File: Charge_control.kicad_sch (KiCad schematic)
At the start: 6 parts, among them Q13 Q_NMOS_SDG, Q14 Q_NMOS_SDG, U3 BQ76200PW

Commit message: update
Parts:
- added C? (x2): 100n, Capacitor_SMD:C_0805_2012Metric, symbol Device:C
- added C?: 100n, symbol Device:C_Small
- added C?: 10n, Capacitor_SMD:C_0805_2012Metric, symbol Device:C
- added D?: D_Zener, symbol Device:D_Zener
- added J4: Conn_01x05, Connector_PinSocket_2.54mm:PinSocket_1x05_P2.54mm_Vertical, symbol Connector_Generic:Conn_01x05
- added Q?: BSS84, Package_TO_SOT_SMD:SOT-23, symbol Transistor_FET:BSS84
- added Q?: Q_NMOS_SDG, symbol Device:Q_NMOS_SDG
- added R67: 0.001, Resistor_SMD:R_Shunt_Vishay_WSKW0612, symbol Device:R_Shunt
- added R?: 110k, Resistor_SMD:R_0805_2012Metric, symbol Device:R
- added R?: 1M, Resistor_SMD:R_0805_2012Metric, symbol Device:R
- added R?: 10k, symbol Device:R
- added R?: 10k, Resistor_SMD:R_0805_2012Metric, symbol Device:R
- added R?: 100, Resistor_SMD:R_0805_2012Metric, symbol Device:R
- added R?: 520k, symbol Device:R
- added R?: 4k7, Resistor_SMD:R_0805_2012Metric, symbol Device:R
- added U?: INA180A3, Package_TO_SOT_SMD:SOT-23-5, symbol FLUX_BMS:INA180
- C22, C23: footprint Capacitor_SMD:C_0603_1608Metric -> Capacitor_SMD:C_0805_2012Metric
- R39: footprint Resistor_SMD:R_0603_1608Metric -> Resistor_SMD:R_0805_2012Metric
- U3: LCSC (none) -> C2868795
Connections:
- net BQ_CHG_EN: now also J4.1 (Pin_1)
- net BQ_CP_EN: now also J4.2 (Pin_2)
- net BQ_DSG_EN: now also J4.3 (Pin_3)
- net BQ_PCHG_EN: now also J4.4 (Pin_4)
- net BQ_PMON_EN: now also J4.5 (Pin_5)
- net GND: now also C?.1, C?.1, C?.1, C?.2, Q?.2 (S), R?.2, R?.2, U?.2 (GND)
- net V+: now reaches Q13.1 (S), R39.1
- net V+: now also D?.1 (K), Q?.2 (D), R?.1
- net at U3.10 (PACKDIV): now also R?.1
- net PACK_V: now reaches U3.11 (PACK)
- net PACK_V: now also C?.2, R?.2
- net PACK+: no longer names the net of Q14.1 (S)
- net PACK+: now also R67.4
- new net: Q?.1 (S), R?.1
- new net: D?.2 (A), Q?.3 (G), R?.1, R?.2
- new net: Q?.3 (D), R?.2
- new net: R67.2, U?.3 (+)
- new net: R67.3, U?.4 (-)
- new net +3V3: C?.1, U?.6 (V+)
- new net BAT_V: C?.2, R?.1, R?.2
- new net BAT_V_EN: Q?.1 (G)
- new net CHARGER+: R67.1, R?.1
- new net CHARGER_V: C?.2, R?.1, R?.2
- no-connect marks 0 -> 2
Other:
- note added: "Moet op de GND van charger zitten"
- note added: "Nodig?? Denk het niet"
- note added: "On resistance of internal FET (R between PACK and PACKDIV) typical 2k5"
- moved on the sheet: C22, C23, Q13, Q14, R39, U3

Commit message: routed most tracks
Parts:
- added TP10, TP9: TestPoint, FLUX-BMS:PAD, symbol Connector:TestPoint
- C40: renamed from C?; footprint Capacitor_SMD:C_0805_2012Metric -> (none)
- Q13, Q14: footprint FLUX-BMS:TRANS_DMP2002UPS-13 -> FLUX-BMS:TRANS_BSC076N06NS3-G
- Q15: renamed from Q?; footprint Package_TO_SOT_SMD:SOT-23 -> (none)
- R67: value 0.001 -> 0.005; footprint Resistor_SMD:R_Shunt_Vishay_WSKW0612 -> Resistor_SMD:R_2512_6332Metric; symbol Device:R_Shunt -> Device:R; LCSC C481535 -> C2903465
- R68, R69, R70, R71: renamed from R?; footprint Resistor_SMD:R_0805_2012Metric -> (none)
- R72: renamed from R?; value 520k -> 470k (was 520k)
- U9: renamed from U?; value INA180A3 -> INA180A2
- gave numbers to parts that had none: 7
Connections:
- net CHARGER+: now also Q14.1 (S), TP9.1; no longer R67.1
- net GND: now also R67.2, U9.4 (-)
- net at U9.3 (+): now also R67.1, TP10.1; no longer R67.2
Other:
- note added: "Nodig?? Denk het niet Calculated from individual cells total sum"
- note removed: "Moet op de GND van charger zitten"
- note removed: "Nodig?? Denk het niet"
- moved on the sheet: C42, U9

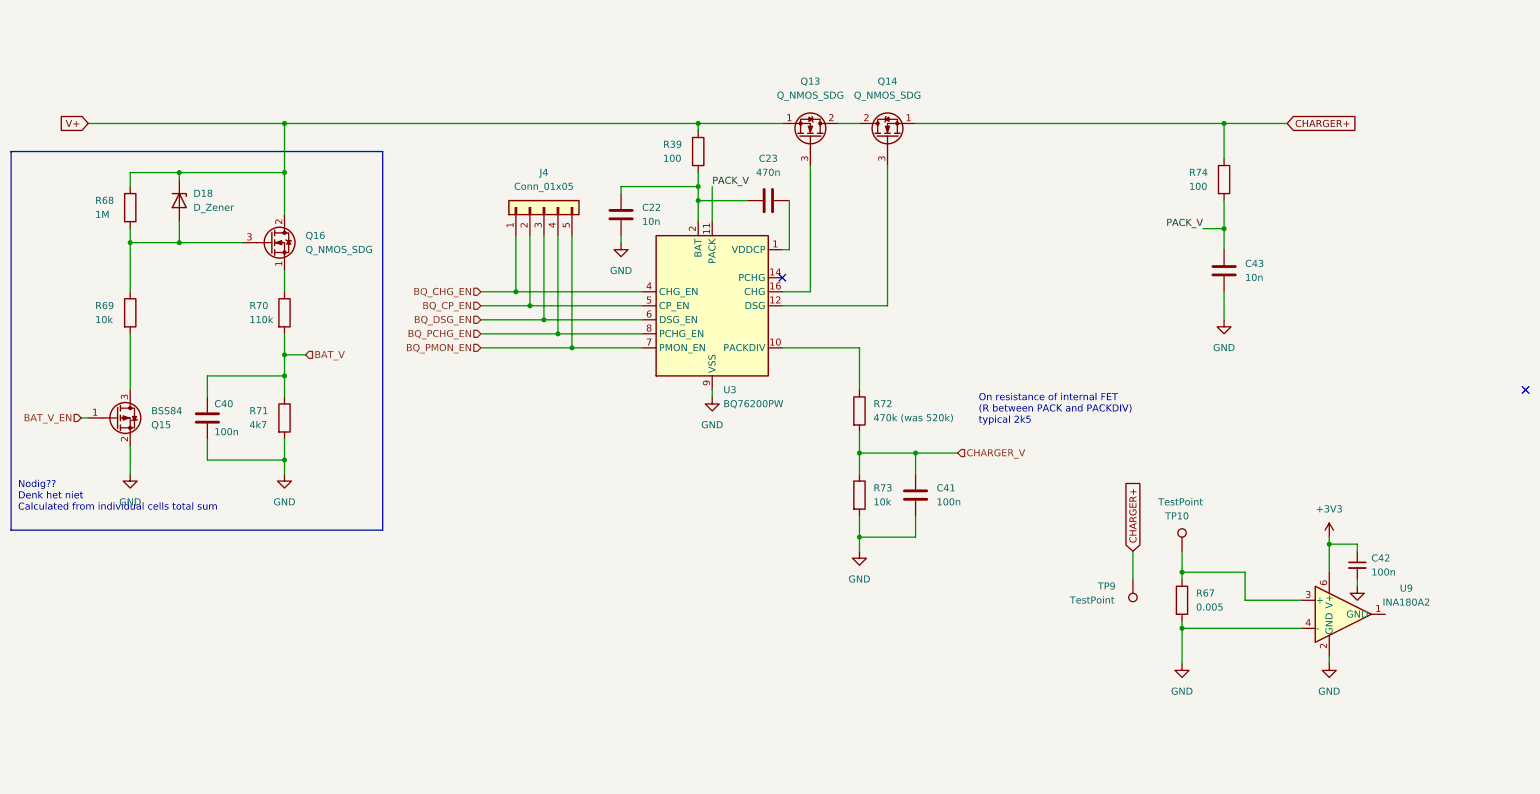
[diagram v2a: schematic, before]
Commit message: new board dimensions
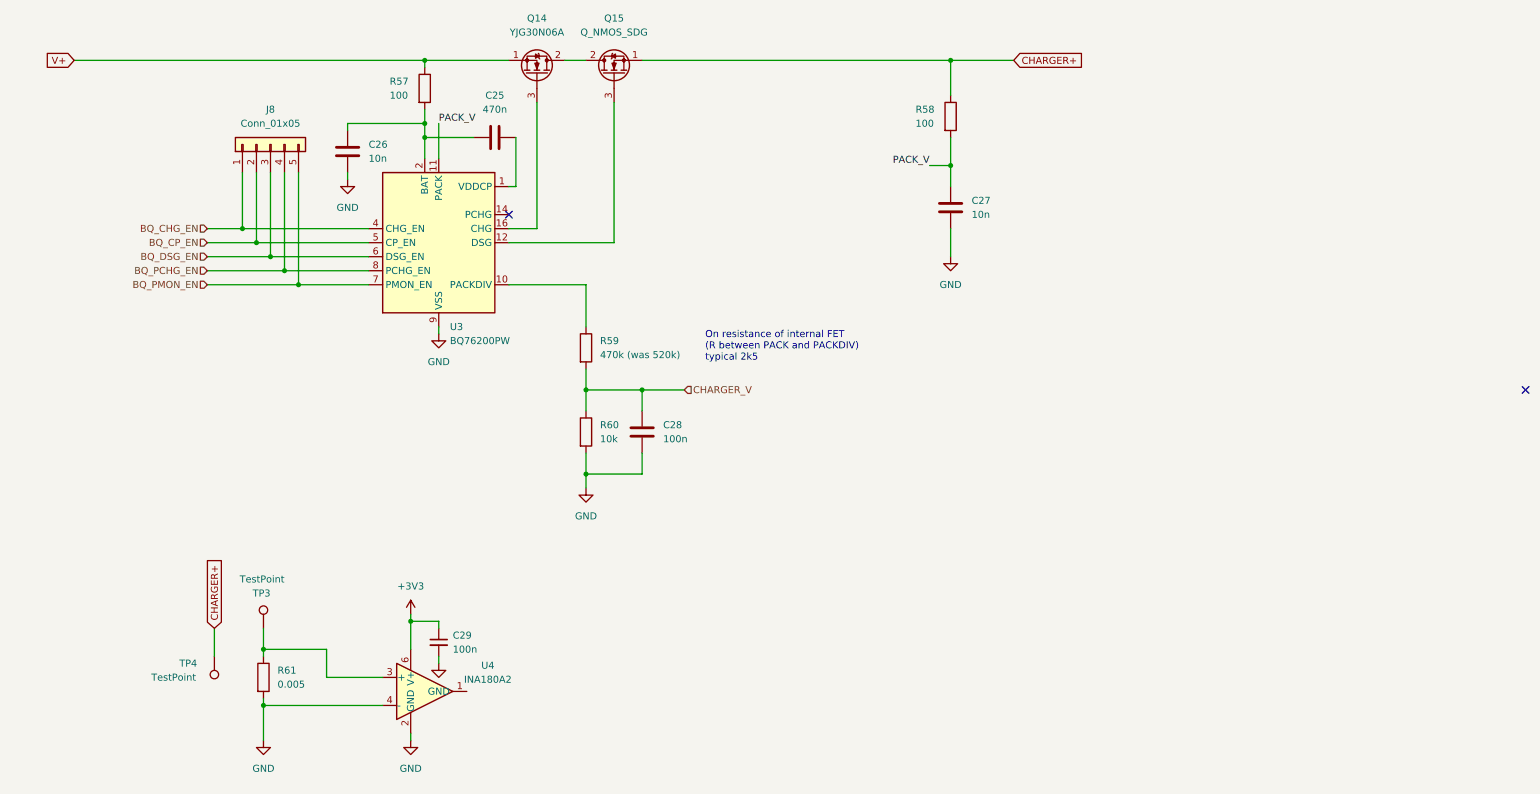
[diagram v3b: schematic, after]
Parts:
- removed C40: 100n, symbol Device:C
- removed D18: D_Zener, symbol Device:D_Zener
- removed Q15: BSS84, symbol Transistor_FET:BSS84
- removed Q16: Q_NMOS_SDG, symbol Device:Q_NMOS_SDG
- removed R68: 1M, symbol Device:R
- removed R69: 10k, symbol Device:R
- removed R70: 110k, symbol Device:R
- removed R71: 4k7, symbol Device:R
- C29: renamed from C42; footprint (none) -> Capacitor_SMD:C_0805_2012Metric
- Q14: renamed from Q13; value Q_NMOS_SDG -> YJG30N06A; LCSC (none) -> C919593
- R59: renamed from R72; footprint (none) -> Resistor_SMD:R_0805_2012Metric
- R60: renamed from R73; footprint (none) -> Resistor_SMD:R_0805_2012Metric
- U3: LCSC C2868795 -> C216213
- U4: renamed from U9; LCSC (none) -> C192764
- renumbered C23 to C25, C22 to C26, C43 to C27, C41 to C28, J4 to J8, Q14 to Q15, R39 to R57, R74 to R58, R67 to R61, TP10 to TP3, TP9 to TP4
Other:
- note removed: "Nodig?? Denk het niet Calculated from individual cells total sum"
- moved on the sheet: C25, C26, C27, C28, C29, J8, Q14, Q15, R57, R58, R59, R60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

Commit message: before meeting
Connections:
- net +3V3: now also U4.5 (VS); no longer U4.6 (V+)
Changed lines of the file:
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@@
     (pin "3")
     (pin "4")
-    (pin "6")
+    (pin "5")
   )
   (symbol (lib_id "Device:C") (at 106.68 55.88 90) (unit 1)

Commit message: almost ready to order
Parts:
- removed J8: Conn_01x05, Connector_PinSocket_2.54mm:PinSocket_1x05_P2.54mm_Vertical, symbol Connector_Generic:Conn_01x05
- added NT1, NT2: NetTie_2, NetTie:NetTie-2_SMD_Pad0.5mm, symbol Device:NetTie_2
- C25: value 470n -> 1u; footprint Capacitor_SMD:C_0805_2012Metric -> Capacitor_SMD:C_0603_1608Metric
- C26, C29: footprint Capacitor_SMD:C_0805_2012Metric -> Capacitor_SMD:C_0603_1608Metric
- Q14: value YJG30N06A -> HYG025N06LS1C2; LCSC C919593 -> C2827231
- Q15: value Q_NMOS_SDG -> HYG025N06LS1C2
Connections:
- net GND: now also NT2.1; no longer U4.4 (-)
- net at R61.1, TP3.1: now also NT1.1; no longer U4.3 (+)
- net CHARGER_CUR: now reaches U4.1
- net BQ_PCHG_EN: no longer names the net of U3.8 (PCHG_EN)
- new net CUR_+: NT1.2, U4.3 (+)
- new net CUR_-: NT2.2, U4.4 (-)
- no-connect marks 2 -> 3
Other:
- moved on the sheet: C29, R61, TP3, TP4, U4

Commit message: before switching to kicad 7
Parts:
- C25: LCSC (none) -> C5673
- C26: LCSC (none) -> C1589
- C27: LCSC (none) -> C1710
- C28: LCSC (none) -> C1711
- C29: LCSC (none) -> C1591
- Q15: LCSC (none) -> C2827231
- R57, R58: LCSC (none) -> C17408
- R59: LCSC (none) -> C17709
- R60: LCSC (none) -> C17414
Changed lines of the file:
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@@
+      (effects (font (size 1.27 1.27)) hide)
+    )
+    (property "LCSC" "C1711" (id 4) (at 133.35 109.22 0)
       (effects (font (size 1.27 1.27)) hide)
     )
@@
     )
     (property "Datasheet" "~" (id 3) (at 80.01 58.42 0)
+      (effects (font (size 1.27 1.27)) hide)
+    )
+    (property "LCSC" "C1589" (id 4) (at 80.01 58.42 0)
       (effects (font (size 1.27 1.27)) hide)
     )
@@
     )
     (property "Datasheet" "~" (id 3) (at 123.19 109.22 0)
+      (effects (font (size 1.27 1.27)) hide)
+    )
+    (property "LCSC" "C17414" (id 4) (at 123.19 109.22 0)
       (effects (font (size 1.27 1.27)) hide)
     )
@@
       (effects (font (size 1.27 1.27)) hide)
     )
+    (property "LCSC" "C2827231" (id 4) (at 128.27 44.45 90)
+      (effects (font (size 1.27 1.27)) hide)
+    )
     (pin "1")
     (pin "2")
@@
       (effects (font (size 1.27 1.27)) hide)
     )
+    (property "LCSC" "C17408" (id 4) (at 189.23 52.07 0)
+      (effects (font (size 1.27 1.27)) hide)
+    )
     (pin "1")
     (pin "2")
@@
       (effects (font (size 1.27 1.27)) hide)
     )
+    (property "LCSC" "C17408" (id 4) (at 93.98 46.99 0)
+      (effects (font (size 1.27 1.27)) hide)
+    )
     (pin "1")
     (pin "2")
@@
     )
     (property "Datasheet" "~" (id 3) (at 123.19 93.98 0)
+      (effects (font (size 1.27 1.27)) hide)
+    )
+    (property "LCSC" "C17709" (id 4) (at 123.19 93.98 0)
       (effects (font (size 1.27 1.27)) hide)
     )
@@
       (effects (font (size 1.27 1.27)) hide)
     )
+    (property "LCSC" "C1591" (id 4) (at 115.57 142.24 0)
+      (effects (font (size 1.27 1.27)) hide)
+    )
     (pin "1")
     (pin "2")
@@
     )
     (property "Datasheet" "~" (id 3) (at 189.23 68.58 0)
+      (effects (font (size 1.27 1.27)) hide)
+    )
+    (property "LCSC" "C1710" (id 4) (at 189.23 68.58 0)
       (effects (font (size 1.27 1.27)) hide)
     )
@@
       (effects (font (size 1.27 1.27)) hide)
     )
+    (property "LCSC" "C5673" (id 4) (at 106.68 55.88 0)
+      (effects (font (size 1.27 1.27)) hide)
+    )

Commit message: V0.2
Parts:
- removed U4: INA180A2, Package_TO_SOT_SMD:SOT-23-5, symbol FLUX_BMS:INA180
- added C40: 10u, Capacitor_SMD:C_0805_2012Metric, symbol Device:C
- added R86, R87: 10k, Resistor_SMD:R_0603_1608Metric, symbol Device:R
- added U4: INA181, Package_TO_SOT_SMD:SOT-23-6, symbol Amplifier_Current:INA181
- C25: LCSC C5673 -> C15849
- C26: LCSC C1589 -> C57112
- C28: LCSC C1711 -> C28233
- C29: LCSC C1591 -> C14663
- Q14, Q15: value HYG025N06LS1C2 -> HYG080N10LS1C2; LCSC C2827231 -> C3011225
- TP3: value TestPoint -> CHARGER-
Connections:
- net +3V3: now also R86.1, U4.6 (V+)
- net CHARGER_CUR: now also U4.1
- net CUR_+: now also U4.3 (+)
- net CUR_-: now also U4.4 (-)
- net GND: now also C40.2, R87.2, U4.2 (GND); no longer NT2.1, R61.2
- net BAT-: now reaches NT1.1, R61.1
- net BAT-: no longer TP3.1
- net CHARGER+ renamed CHG+
- net CHG+: no longer R58.1
- net V+ renamed BAT+
- net BAT+: now also R58.1
- new net 1V65: C40.1, R86.2, R87.1, U4.5 (REF)
- new net CHG-: NT2.1, R61.2, TP3.1
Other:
- moved on the sheet: C27, Q15, R58, TP4
